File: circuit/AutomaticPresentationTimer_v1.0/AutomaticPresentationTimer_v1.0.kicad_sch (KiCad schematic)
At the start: 19 parts, among them J1 Conn_01x05, J2 Conn_01x03, J3 ZHO-0420S-05A4.5(5V), J4 ディスプレイモジュール, Q1 2SK4017, U1 Pico

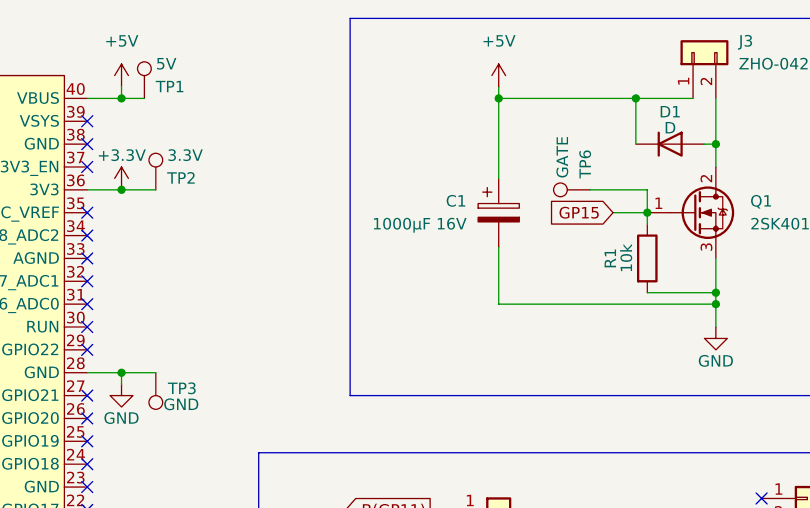
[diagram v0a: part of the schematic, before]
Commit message: コンデンサの名称を修正
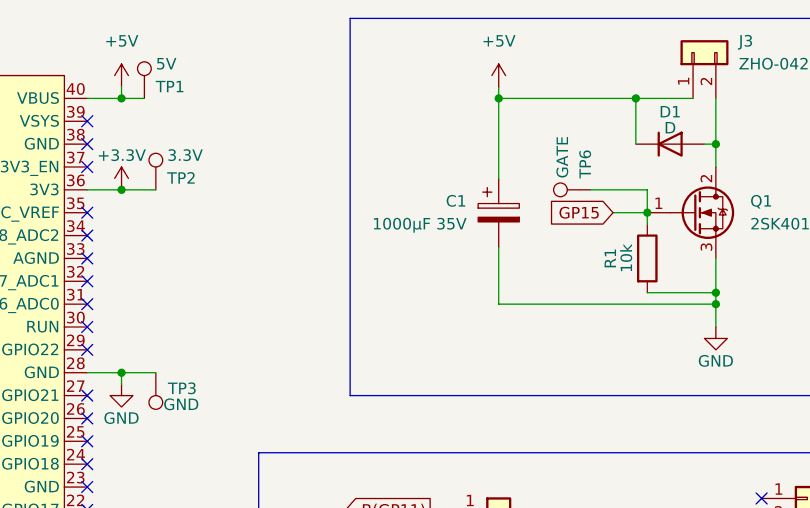
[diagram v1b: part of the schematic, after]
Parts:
- C1: value 1000µF 16V -> 1000µF 35V
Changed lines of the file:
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@@
 			)
 		)
-		(property "Value" "1000µF 16V"
+		(property "Value" "1000µF 35V"
 			(at 176.784 74.93 0)
 			(effects
